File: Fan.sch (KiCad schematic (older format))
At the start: 0 parts

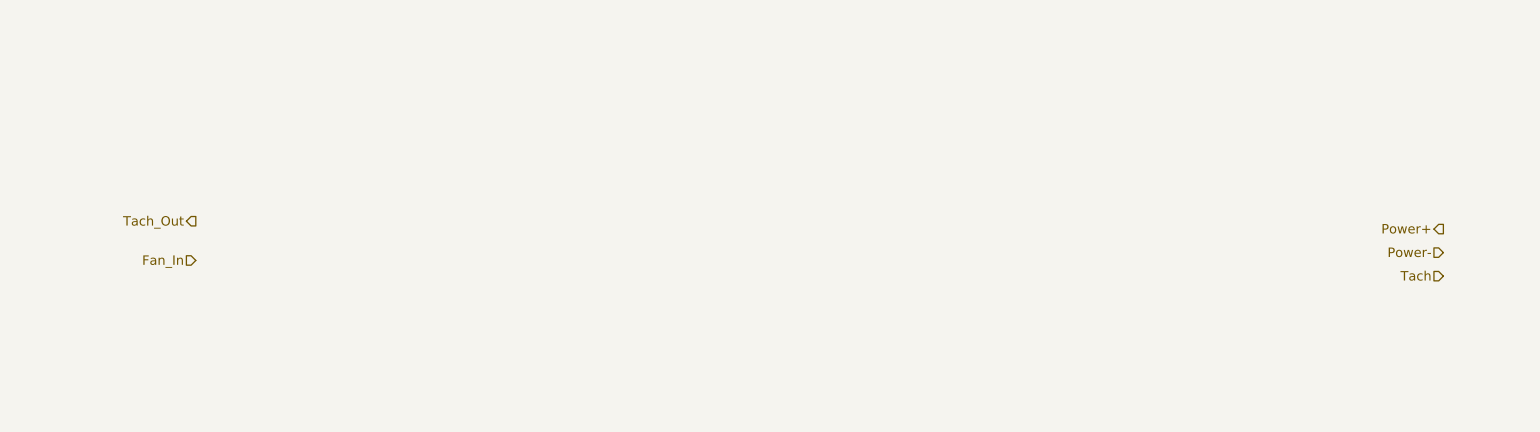
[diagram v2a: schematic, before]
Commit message: Added Fan Schematic
Added generic schematic for fan controller
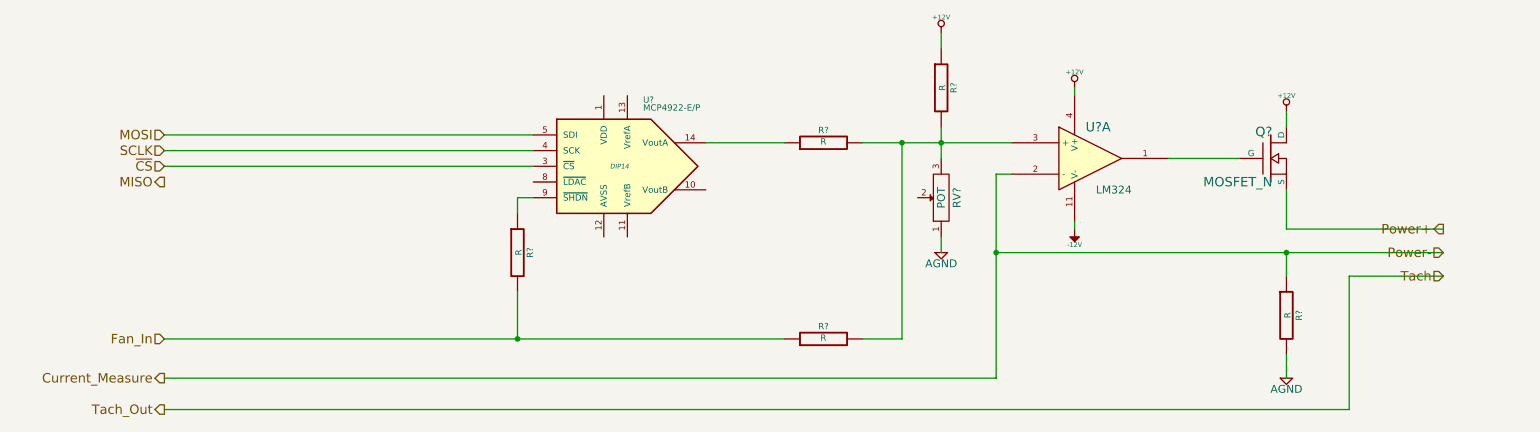
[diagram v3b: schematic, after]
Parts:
- added Q?: MOSFET_N, ~, symbol MOSFET_N
- added R? (x5): R, ~, symbol R
- added RV?: POT, ~, symbol POT
- added U?: LM324, symbol LM324
- added U?: MCP4922-E/P, DIP14, symbol MCP4922-E/P
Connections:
- net Fan_In: now also R?.1, R?.2
- net Power+: now also Q?.S
- new net: Q?.G, U?.1
- new net: R?.2, R?.2, R?.2, RV?.3, U?.3 (+)
- new net: R?.1, U?.14 (VoutA)
- new net: R?.1, U?.9 (~SHDN~)
- new net +12V: Q?.D, R?.1, U?.4 (V+)
- new net -12V: U?.11 (V-)
- new net AGND: R?.2, RV?.1
- new net Current_Measure: R?.1, U?.2 (-)
- new net MOSI: U?.5 (SDI)
- new net SCLK: U?.4 (SCK)
- new net ~CS: U?.3 (~CS~)

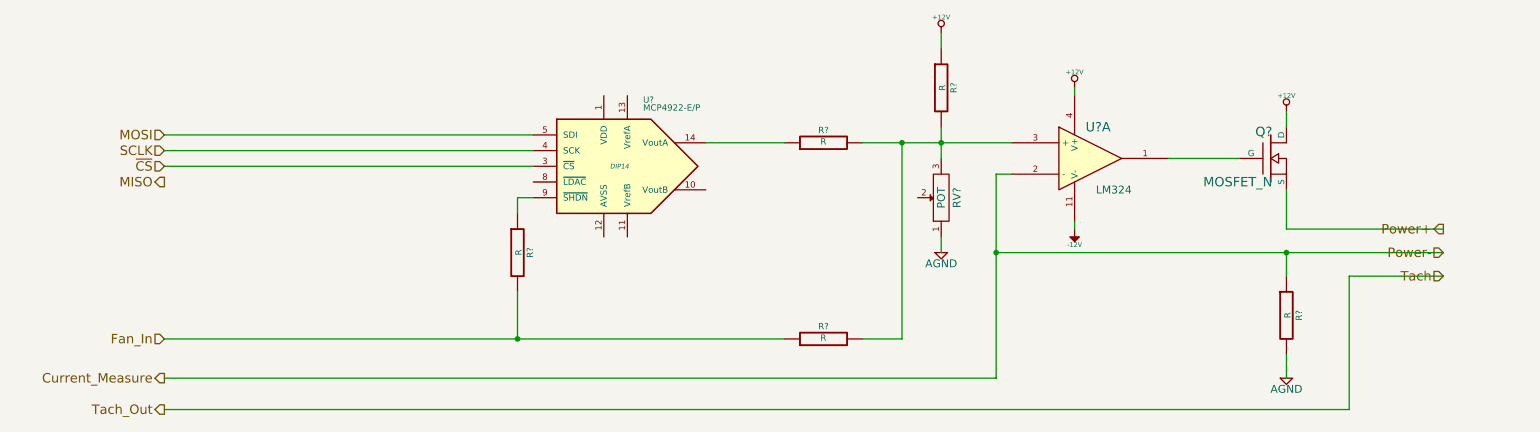
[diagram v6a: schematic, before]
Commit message: Added connections to Terminal Block
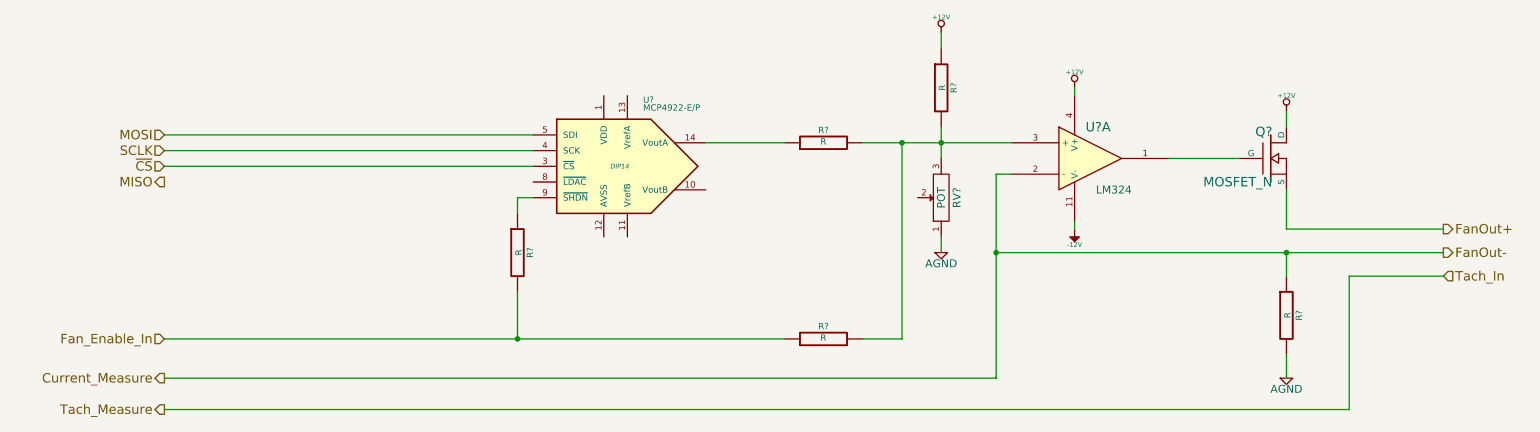
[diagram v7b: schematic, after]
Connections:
- net Fan_In renamed Fan_Enable_In
- net Power+ renamed FanOut+
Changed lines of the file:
@@
 $Descr A4 11693 8268
 encoding utf-8
-Sheet 6 9
+Sheet 5 9
 Title ""
 Date "11 oct 2013"
@@
 Comment4 ""
 $EndDescr
-Text HLabel 9650 2000 0    60   Output ~ 0
-Power+
-Text HLabel 9650 2150 0    60   Input ~ 0
-Power-
-Text HLabel 9650 2300 0    60   Input ~ 0
-Tach
+Text HLabel 9650 2000 2    60   Output ~ 0
+FanOut+
+Text HLabel 9650 2150 2    60   Output ~ 0
+FanOut-
+Text HLabel 9650 2300 2    60   Input ~ 0
+Tach_In
 Text HLabel 1500 3150 0    60   Output ~ 0
-Tach_Out
+Tach_Measure
 Text HLabel 1500 2700 0    60   Input ~ 0
-Fan_In
+Fan_Enable_In
 $Comp
 L LM324 U?
